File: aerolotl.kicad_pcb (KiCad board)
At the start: 2 copper layers, 9 parts, among them SW1 SW_Nidec_CAS-120A1, U1 STM32H755ZIT6, U10 LMR51430XFDDCR, U2 BMP581, U3 BNO085, U4 ADXL345BCCZ-RL7, U6 USBLC6-2P6, U8 FT230XQ, U9 AMS1117-3.3

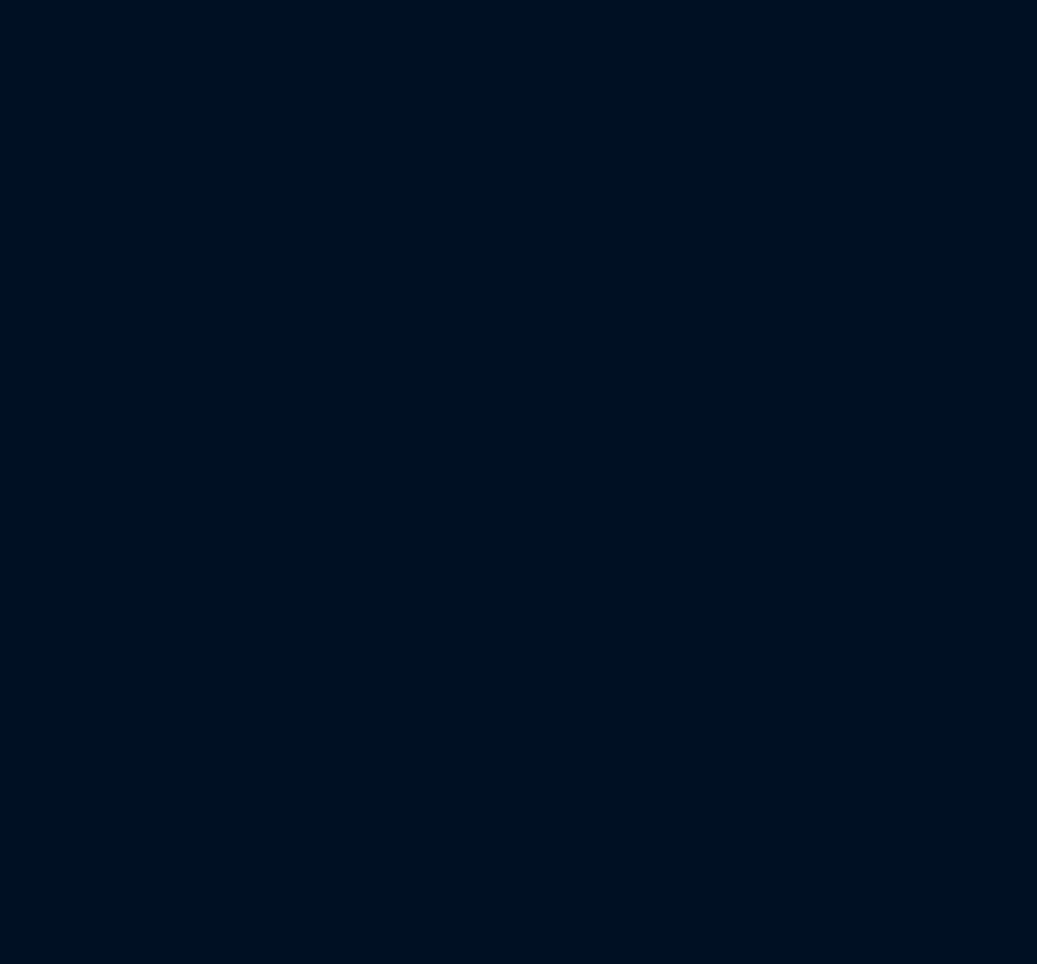
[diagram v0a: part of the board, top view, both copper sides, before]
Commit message: Refactor repository: consolidate custom libraries, move hierarchical sheets, and clean up root directory
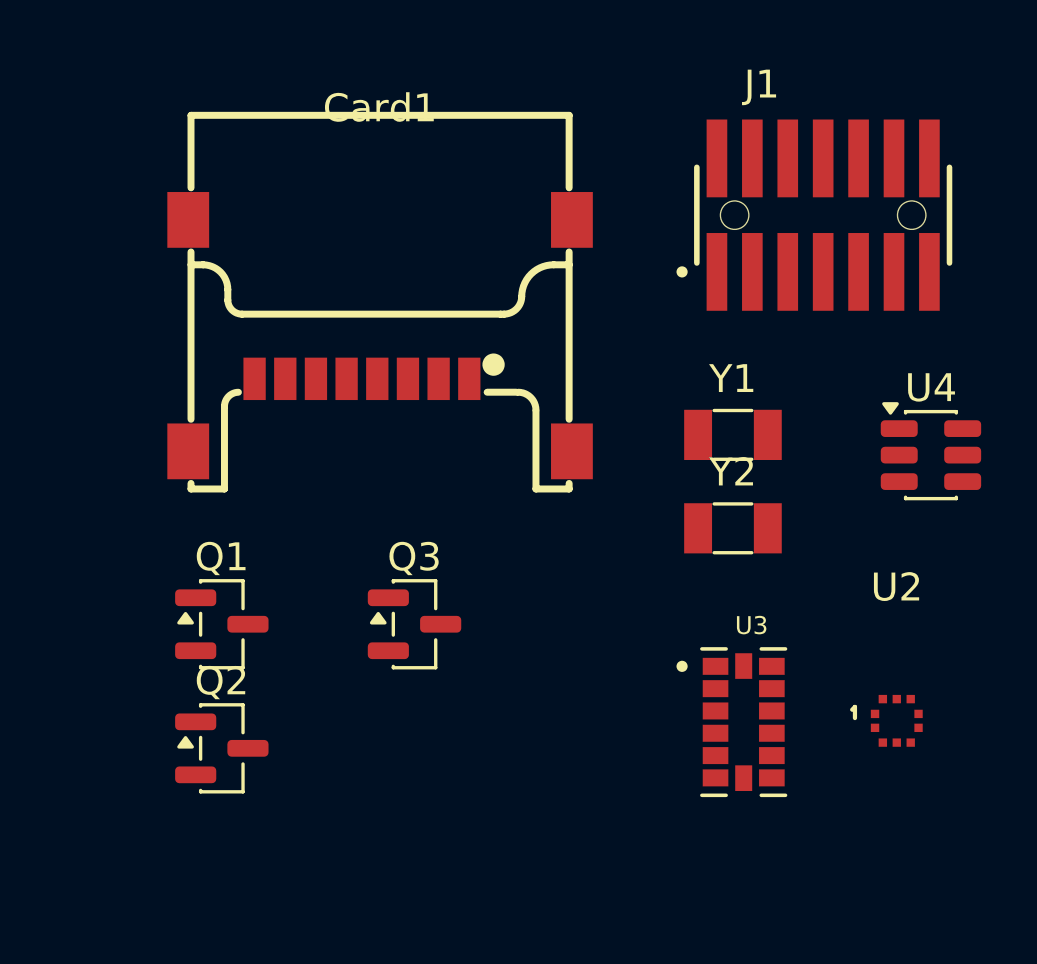
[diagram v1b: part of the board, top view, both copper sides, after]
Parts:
- added Card1: TF-102-15, TF-SMD_TF-102-15:TF-SMD_TF-102-15, F.Cu at (207.1, 57.7)
- added J1: SWD, FTSH-107-01-L-DV-K-A:SAMTEC_FTSH-107-01-L-DV-K-A, F.Cu at (223.0, 53.3)
- added Q1: AO3400A, Package_TO_SOT_SMD:SOT-23, F.Cu at (201.4, 68.0)
- added Q2: AO3400A, Package_TO_SOT_SMD:SOT-23, F.Cu at (201.4, 72.5)
- added Q3: AO3400A, Package_TO_SOT_SMD:SOT-23, F.Cu at (208.3, 68.0)
- added U2: BMP581, aerolotl_custom:LGA-10_L2.0-W2.0-P0.50-TL_BMP581, F.Cu at (225.6, 71.5)
- added U3: ADXL345BCCZ-RL7, ADXL345BCCZ-RL7:PQFN80P500X300X100-14N, F.Cu at (220.1, 71.5)
- added U4: LMR51430XFDDCR, Package_TO_SOT_SMD:SOT-23-6, F.Cu at (226.9, 62.0)
- added Y1: 25M, Crystal:Crystal_SMD_3215-2Pin_3.2x1.5mm, F.Cu at (219.8, 61.2)
- added Y2: Crystal, Crystal:Crystal_SMD_3215-2Pin_3.2x1.5mm, F.Cu at (219.8, 64.6)
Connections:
- net /Power/USB_DN renamed /Power/USB_DM
- U1 pad 10: unconnected-(U1B-PC14-Pad10) -> /MCU/LS_OSC_A
- U1 pad 100: unconnected-(U1B-PA11-Pad100) -> /MCU/USB_D_M
- U1 pad 101: unconnected-(U1B-PA12-Pad101) -> /MCU/USB_D_P
- U1 pad 102: unconnected-(U1B-PA13-Pad102) -> /MCU/SWDIO
- U1 pad 107: unconnected-(U1B-PA14-Pad107) -> /MCU/SWCLK
- U1 pad 109: unconnected-(U1B-PC10-Pad109) -> /MCU/SDMMC1.D2
- U1 pad 11: unconnected-(U1B-PC15-Pad11) -> /MCU/LS_OSC_B
- U1 pad 110: unconnected-(U1B-PC11-Pad110) -> /MCU/SDMMC1.D3
- U1 pad 111: unconnected-(U1B-PC12-Pad111) -> /MCU/SDMMC1.CK
- U1 pad 114: unconnected-(U1B-PD2-Pad114) -> /MCU/SDMMC1.CMD
- U1 pad 25: unconnected-(U1B-PH0-Pad25) -> /MCU/HS_OSC_A
- U1 pad 26: unconnected-(U1B-PH1-Pad26) -> /MCU/HS_OSC_B
- U1 pad 52: /MCU/BMP.INT -> unconnected-(U1B-PF11-Pad52)
- U1 pad 53: /MCU/BMP.SCK -> unconnected-(U1B-PF14-Pad53)
- U1 pad 54: /MCU/BMP.SDA -> unconnected-(U1B-PF15-Pad54)
- U1 pad 95: unconnected-(U1B-PC8-Pad95) -> /MCU/SDMMC1.D0
- U1 pad 96: unconnected-(U1B-PC9-Pad96) -> /MCU/SDMMC1.D1
- U6 pad 4: /Power/FTDI_USB_DP -> /MCU/USB_D_P
- U6 pad 6: /Power/FTDI_USB_DN -> /MCU/USB_D_M

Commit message: Fixed up power, added remaining to do
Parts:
- moved U4 16.8 mm to (243.4, 65.0)
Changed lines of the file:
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@@
 	(footprint "Package_TO_SOT_SMD:SOT-23-6"
 		(layer "F.Cu")
-		(at 226.8625 61.95)
+		(at 243.3625 64.95)
 		(descr "SOT, 6 Pin (JEDEC MO-178 Var AB https://www.jedec.org/document_search?search_api_views_fulltext=MO-178), generated with kicad-footprint-generator ipc_gullwing_generator.py")
 		(tags "SOT TO_SOT_SMD")
@@
 			(hide yes)
 			(effects
+				(font
+					(size 1.27 1.27)
+					(thickness 0.15)
+				)
+			)
+		)
+		(property "LCSC" "C5219260"
+			(at 0 0 0)
+			(layer "F.SilkS")
+			(hide yes)
+			(effects

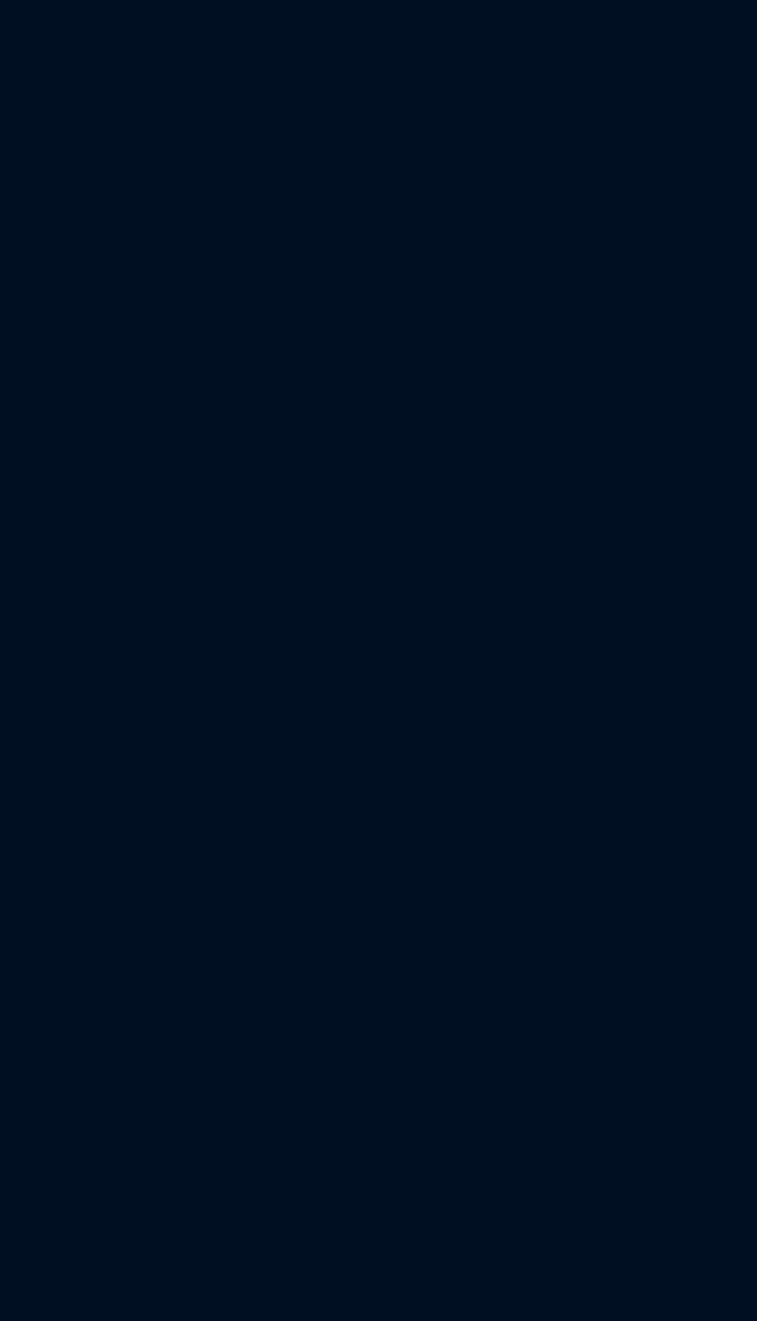
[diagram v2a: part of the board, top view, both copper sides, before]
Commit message: polished up circuit, added new 16.8V to 7.4V step down circuit components
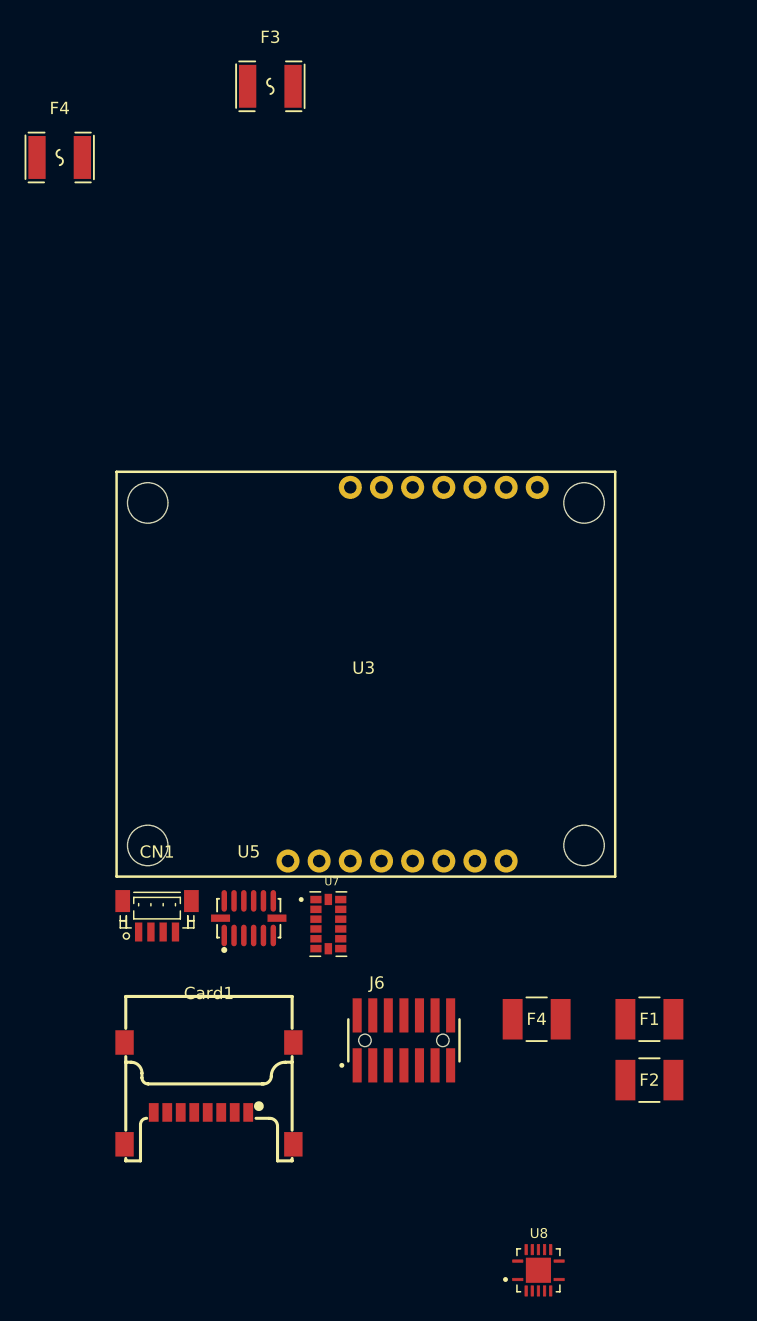
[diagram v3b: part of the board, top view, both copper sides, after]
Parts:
- added CN1: StemmaQT, aerolotl_custom:CONN-SMD_BM04B-SRSS-TB, F.Cu at (54.4, 92.7)
- added Card1: TF-102-15_SD_read, aerolotl_custom:TF-SMD_TF-102-15, F.Cu at (58.6, 107.1)
- added F1: 1812L150/24MR, aerolotl_custom:FUSE_1812L150&slash_24_LTF, F.Cu at (94.5, 101.0)
- added F2: 1812L150/24MR, aerolotl_custom:FUSE_1812L150&slash_24_LTF, F.Cu at (94.5, 106.0)
- added F3: 1812L300/24SLER, aerolotl_custom:F1812, F.Cu at (63.6, 25.0)
- added F4: 1812L300/24SLER, aerolotl_custom:F1812, F.Cu at (46.5, 30.8)
- added F4: 1812L150/24MR, aerolotl_custom:FUSE_1812L150&slash_24_LTF, F.Cu at (85.4, 101.0)
- added J6: FTSH-107-STDC14, aerolotl_custom:SAMTEC_FTSH-107-01-L-DV-K-A, F.Cu at (74.5, 102.8)
- added U3: SparkfunM9N, aerolotl_custom:SparkfunM9N, F.Cu at (71.3, 72.9)
- added U5: ADXL375BCCZ-RL7, aerolotl_custom:LGA-14_L5.0-W3.0-P0.80-BL, F.Cu at (61.9, 92.8)
- added U7: ADXL345BCCZ-RL7, aerolotl_custom:ADXL345, F.Cu at (68.4, 93.3)
- added U8: TPS54620RGYR, aerolotl_custom:TPS54620_7v4buck, F.Cu at (85.5, 121.5)
- Y2: value Crystal -> 32k768
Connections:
- net /Indicators/Buzzer renamed /Indicators/BUZZER
- net Net-(U4-EN) renamed +12V
- SW1 pad 3: VCC -> +3V3
- U1 pad 102: /MCU/SWDIO -> /Debugger/T_SWDIO
- U1 pad 107: /MCU/SWCLK -> /Debugger/T_SWCLK
- U1 pad 130: unconnected-(U1B-PB3-Pad130) -> /Debugger/T_SWO
- U1 pad 44: unconnected-(U1B-PA5-Pad44) -> /IMUs/ADXL345.SCLK
- U1 pad 45: unconnected-(U1B-PA6-Pad45) -> /IMUs/ADXL345.SDI
- U1 pad 46: unconnected-(U1B-PA7-Pad46) -> /IMUs/ADXL345.SDO
- U1 pad 98: /MCU/USART1_TX -> /Debugger/T_VCP_RX
- U1 pad 99: /MCU/USART1_RX -> /Debugger/T_VCP_TX
- U2 pad 1: VDD -> Net-(U2-VDDIO)
- U2 pad 10: VDD -> Net-(U2-VDD)
- U2 pad 2: /IMUs/BMP.SCK -> /IMUs/ADXL345.SCLK
- U2 pad 4: /IMUs/BMP.MOSI -> /IMUs/ADXL345.SDO
- U2 pad 5: /IMUs/BMP.MISO -> /IMUs/ADXL345.SDI

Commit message: some footprints assigned
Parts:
- moved Y2 8.33 mm to (227.5, 61.5)
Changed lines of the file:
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@@
 	(footprint "Crystal:Crystal_SMD_3215-2Pin_3.2x1.5mm"
 		(layer "F.Cu")
-		(at 219.7625 64.575)
+		(at 227.5 61.5)
 		(descr "SMD Crystal FC-135 https://support.epson.biz/td/api/doc_check.php?dl=brief_FC-135R_en.pdf")
 		(tags "SMD SMT Crystal")
@@
 					(thickness 0.15)
 				)
+			)
+		)
+		(property "LCSC" "C32346"
+			(at 0 0 0)
+			(layer "F.SilkS")
+			(hide yes)
+			(effects
+				(font
+					(size 1.27 1.27)
+					(thickness 0.15)
+				)
